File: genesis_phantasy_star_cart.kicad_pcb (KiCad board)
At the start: 4 copper layers, 83.7 x 63.7 mm, 12 parts, among them J1 Sega_MegaDrive_Cart_Conn, J2 Batt, U1 315-5235, U2 MPR-11711, U3 MB8464A, U4 BQ2201SN

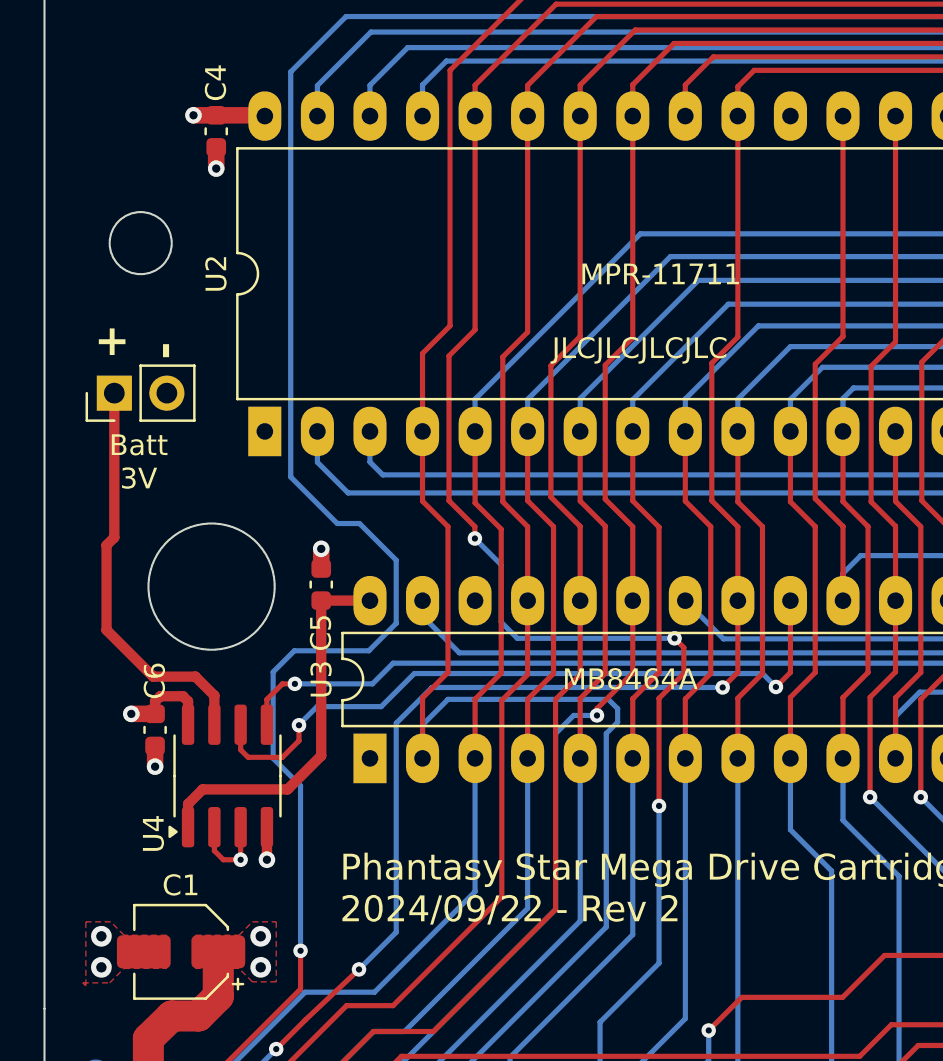
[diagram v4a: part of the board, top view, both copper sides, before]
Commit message: Convert backup battery to proper footprint
* Backup battery is now using a proper footprint for a CR2032 with
  solder tabs. Kapton tape will be needed between battery and pins on
  the backside of the board.
* Converted battery pin header to be a secondary battery to
  maintain the SRAM while changing the primary battery. Added a pulldown
  to this to keep the supervisor happy while the seconary is not
  connected.
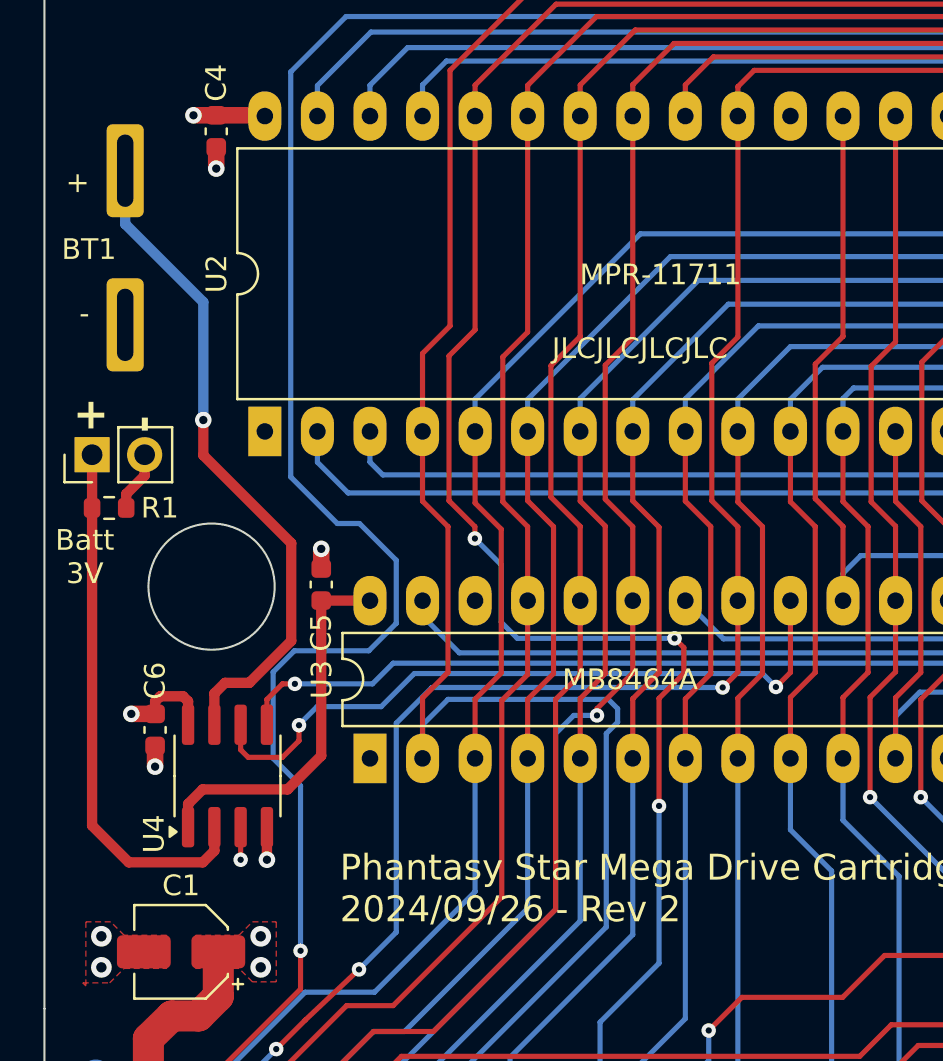
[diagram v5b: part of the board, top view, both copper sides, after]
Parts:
- added BT1: CR2032, Custom:CR2032L-F1N, B.Cu at (72.0, 69.3)
- added R1: 10K, Resistor_SMD:R_0603_1608Metric, F.Cu at (71.2, 85.6)
- moved J2 3.16 mm to (70.4, 83.0)
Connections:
- J2 pad 1: /BATT+ -> /BATT2+
- U4 pad 2: GND -> /BATT2+
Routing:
- net /BATT2+: track 0.00 -> 25.9 mm
- net /BATT+: track 19.5 -> 32.3 mm, vias 0 -> 1
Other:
- outline, holes or cut-outs redrawn
- board text added: "- +"
- board text added: "Phantasy Star Mega Drive Cartridge 2024/09/26 - Rev 2"
- board text removed: "Phantasy Star Mega Drive Cartridge 2024/09/22 - Rev 2"
